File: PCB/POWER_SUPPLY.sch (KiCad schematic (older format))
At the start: 12 parts

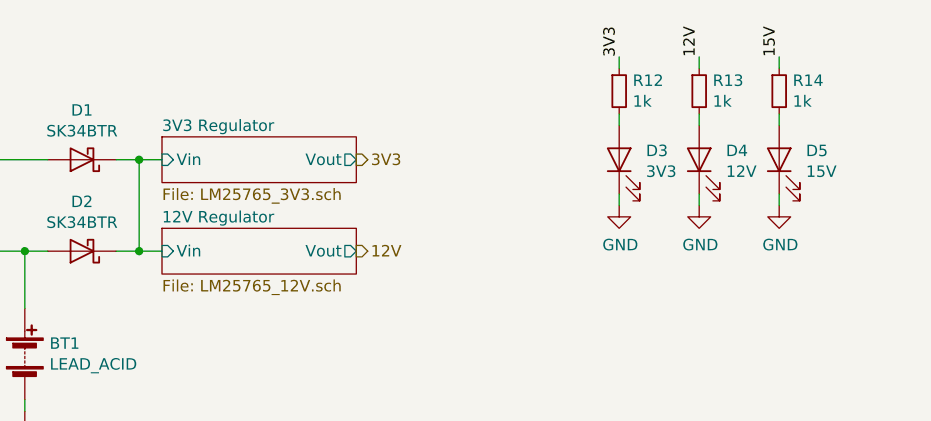
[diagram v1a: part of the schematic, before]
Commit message: Replaced 3v3 regulator with 5v
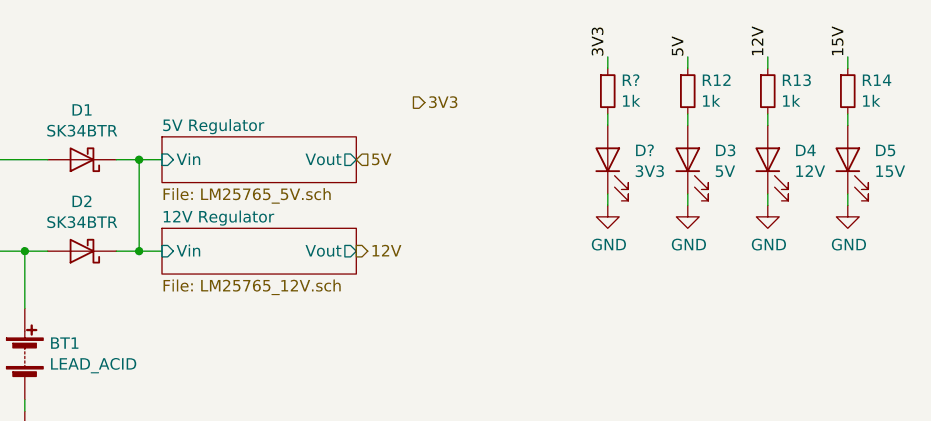
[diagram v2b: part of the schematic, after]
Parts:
- added D?: 3V3, symbol Device:LED
- added R?: 1k, symbol Device:R_Small
- D3: value 3V3 -> 5V
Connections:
- net 3V3: now also R?.1; no longer R12.1
- net GND: now also D?.1 (K)
- new net: D?.2 (A), R?.2
- new net 5V: R12.1
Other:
- moved on the sheet: D3, D4, D5, R12, R13, R14
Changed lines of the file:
@@
 $Descr A4 11693 8268
 encoding utf-8
-Sheet 9 25
+Sheet 10 25
 Title ""
 Date ""
@@
 Wire Wire Line
 	5600 3200 5700 3200
-Text HLabel 7050 2800 2    50   Output ~ 0
+Text HLabel 7300 2550 2    50   Output ~ 0
 3V3
 $Sheet
 S 6200 2700 850  200
 U 5E9C913B
-F0 "3V3 Regulator" 50
-F1 "LM25765_3V3.sch" 50
+F0 "5V Regulator" 50
+F1 "LM25765_5V.sch" 50
 F2 "Vout" O R 7050 2800 50
 F3 "Vin" I L 6200 2800 50
@@
 L Device:LED D3
 U 1 1 5E8B2580
-P 8200 2800
-F 0 "D3" V 8239 2683 50  0000 R CNN
-F 1 "3V3" V 8148 2683 50  0000 R CNN
-F 2 "" H 8200 2800 50  0001 C CNN
-F 3 "" H 8200 2800 50  0001 C CNN
-	1    8200 2800
+P 8500 2800
+F 0 "D3" V 8539 2683 50  0000 R CNN
+F 1 "5V" V 8448 2683 50  0000 R CNN
+F 2 "" H 8500 2800 50  0001 C CNN
+F 3 "" H 8500 2800 50  0001 C CNN
+	1    8500 2800
 	0    -1   -1   0
 $EndComp
@@
 L Device:R_Small R12
 U 1 1 5E8B32F4
-P 8200 2500
-F 0 "R12" H 8259 2546 50  0000 L CNN
-F 1 "1k" H 8259 2455 50  0000 L CNN
-F 2 "" H 8200 2500 50  0001 C CNN
-F 3 "" H 8200 2500 50  0001 C CNN
-	1    8200 2500
-	1    0    0    -1
-$EndComp
-Wire Wire Line
-	8200 2600 8200 2650
+P 8500 2500
+F 0 "R12" H 8559 2546 50  0000 L CNN
+F 1 "1k" H 8559 2455 50  0000 L CNN
+F 2 "" H 8500 2500 50  0001 C CNN
+F 3 "" H 8500 2500 50  0001 C CNN
+	1    8500 2500
+	1    0    0    -1
+$EndComp
+Wire Wire Line
+	8500 2600 8500 2650
 $Comp
 L power:GND #PWR067
 U 1 1 5E8B38F1
-P 8200 3000
-F 0 "#PWR067" H 8200 2750 50  0001 C CNN
-F 1 "GND" H 8205 2827 50  0000 C CNN
-F 2 "" H 8200 3000 50  0001 C CNN
-F 3 "" H 8200 3000 50  0001 C CNN
-	1    8200 3000
-	1    0    0    -1
-$EndComp
-Wire Wire Line
-	8200 2950 8200 3000
+P 8500 3000
+F 0 "#PWR067" H 8500 2750 50  0001 C CNN
+F 1 "GND" H 8505 2827 50  0000 C CNN
+F 2 "" H 8500 3000 50  0001 C CNN
+F 3 "" H 8500 3000 50  0001 C CNN
+	1    8500 3000
+	1    0    0    -1
+$EndComp
+Wire Wire Line
+	8500 2950 8500 3000
 $Comp
 L Device:LED D4
 U 1 1 5E8B5AE6
-P 8550 2800
-F 0 "D4" V 8589 2683 50  0000 R CNN
-F 1 "12V" V 8498 2683 50  0000 R CNN
-F 2 "" H 8550 2800 50  0001 C CNN
-F 3 "" H 8550 2800 50  0001 C CNN
-	1    8550 2800
+P 8850 2800
+F 0 "D4" V 8889 2683 50  0000 R CNN
+F 1 "12V" V 8798 2683 50  0000 R CNN
+F 2 "" H 8850 2800 50  0001 C CNN
+F 3 "" H 8850 2800 50  0001 C CNN
+	1    8850 2800
 	0    -1   -1   0
 $EndComp
@@
 L Device:R_Small R13
 U 1 1 5E8B5AEC
-P 8550 2500
-F 0 "R13" H 8609 2546 50  0000 L CNN
-F 1 "1k" H 8609 2455 50  0000 L CNN
-F 2 "" H 8550 2500 50  0001 C CNN
-F 3 "" H 8550 2500 50  0001 C CNN
-	1    8550 2500
-	1    0    0    -1
-$EndComp
-Wire Wire Line
-	8550 2600 8550 2650
+P 8850 2500
+F 0 "R13" H 8909 2546 50  0000 L CNN
+F 1 "1k" H 8909 2455 50  0000 L CNN
+F 2 "" H 8850 2500 50  0001 C CNN
+F 3 "" H 8850 2500 50  0001 C CNN
+	1    8850 2500
+	1    0    0    -1
+$EndComp
+Wire Wire Line
+	8850 2600 8850 2650
 $Comp
 L power:GND #PWR068
 U 1 1 5E8B5AF3
-P 8550 3000
-F 0 "#PWR068" H 8550 2750 50  0001 C CNN
-F 1 "GND" H 8555 2827 50  0000 C CNN
-F 2 "" H 8550 3000 50  0001 C CNN
-F 3 "" H 8550 3000 50  0001 C CNN
-	1    8550 3000
-	1    0    0    -1
-$EndComp
-Wire Wire Line
-	8550 2950 8550 3000
-Text Label 8200 2350 1    50   ~ 0
-3V3
-Wire Wire Line
-	8200 2350 8200 2400
-Text Label 8550 2350 1    50   ~ 0
+P 8850 3000
+F 0 "#PWR068" H 8850 2750 50  0001 C CNN
+F 1 "GND" H 8855 2827 50  0000 C CNN
+F 2 "" H 8850 3000 50  0001 C CNN
+F 3 "" H 8850 3000 50  0001 C CNN
+	1    8850 3000
+	1    0    0    -1
+$EndComp
+Wire Wire Line
+	8850 2950 8850 3000
+Text Label 8500 2350 1    50   ~ 0
+5V
+Wire Wire Line
+	8500 2350 8500 2400
+Text Label 8850 2350 1    50   ~ 0
 12V
 Wire Wire Line
-	8550 2350 8550 2400
+	8850 2350 8850 2400
 Connection ~ 6100 3200
 Wire Wire Line
@@
 L Device:LED D5
 U 1 1 5E8B6ACE
-P 8900 2800
-F 0 "D5" V 8939 2683 50  0000 R CNN
-F 1 "15V" V 8848 2683 50  0000 R CNN
-F 2 "" H 8900 2800 50  0001 C CNN
-F 3 "" H 8900 2800 50  0001 C CNN
-	1    8900 2800
+P 9200 2800
+F 0 "D5" V 9239 2683 50  0000 R CNN
+F 1 "15V" V 9148 2683 50  0000 R CNN
+F 2 "" H 9200 2800 50  0001 C CNN
+F 3 "" H 9200 2800 50  0001 C CNN
+	1    9200 2800
 	0    -1   -1   0
 $EndComp
@@
 L Device:R_Small R14
 U 1 1 5E8B6AD4
-P 8900 2500
-F 0 "R14" H 8959 2546 50  0000 L CNN
-F 1 "1k" H 8959 2455 50  0000 L CNN
-F 2 "" H 8900 2500 50  0001 C CNN
-F 3 "" H 8900 2500 50  0001 C CNN
-	1    8900 2500
-	1    0    0    -1
-$EndComp
-Wire Wire Line
-	8900 2600 8900 2650
+P 9200 2500
+F 0 "R14" H 9259 2546 50  0000 L CNN
+F 1 "1k" H 9259 2455 50  0000 L CNN
+F 2 "" H 9200 2500 50  0001 C CNN
+F 3 "" H 9200 2500 50  0001 C CNN
+	1    9200 2500
+	1    0    0    -1
+$EndComp
+Wire Wire Line
+	9200 2600 9200 2650
 $Comp
 L power:GND #PWR069
 U 1 1 5E8B6ADB
-P 8900 3000
-F 0 "#PWR069" H 8900 2750 50  0001 C CNN
-F 1 "GND" H 8905 2827 50  0000 C CNN
-F 2 "" H 8900 3000 50  0001 C CNN
-F 3 "" H 8900 3000 50  0001 C CNN
-	1    8900 3000
-	1    0    0    -1
-$EndComp
-Wire Wire Line
-	8900 2950 8900 3000
-Text Label 8900 2350 1    50   ~ 0
+P 9200 3000
+F 0 "#PWR069" H 9200 2750 50  0001 C CNN
+F 1 "GND" H 9205 2827 50  0000 C CNN
+F 2 "" H 9200 3000 50  0001 C CNN
+F 3 "" H 9200 3000 50  0001 C CNN
+	1    9200 3000
+	1    0    0    -1
+$EndComp
+Wire Wire Line
+	9200 2950 9200 3000
+Text Label 9200 2350 1    50   ~ 0
 15V
 Wire Wire Line
-	8900 2350 8900 2400
+	9200 2350 9200 2400
 Text Label 3750 2800 0    50   ~ 0
 15V
+Text HLabel 7050 2800 2    50   Input ~ 0
+5V
+$Comp
+L Device:LED D?
+U 1 1 5E8FE8F5
+P 8150 2800
+F 0 "D?" V 8189 2683 50  0000 R CNN
+F 1 "3V3" V 8098 2683 50  0000 R CNN
+F 2 "" H 8150 2800 50  0001 C CNN
+F 3 "" H 8150 2800 50  0001 C CNN
+	1    8150 2800
+	0    -1   -1   0
+$EndComp
+$Comp
+L Device:R_Small R?
+U 1 1 5E8FE8FB
+P 8150 2500
+F 0 "R?" H 8209 2546 50  0000 L CNN
+F 1 "1k" H 8209 2455 50  0000 L CNN
+F 2 "" H 8150 2500 50  0001 C CNN
+F 3 "" H 8150 2500 50  0001 C CNN
+	1    8150 2500
+	1    0    0    -1
+$EndComp
+Wire Wire Line
+	8150 2600 8150 2650
+$Comp
+L power:GND #PWR?
+U 1 1 5E8FE902
+P 8150 3000
+F 0 "#PWR?" H 8150 2750 50  0001 C CNN
+F 1 "GND" H 8155 2827 50  0000 C CNN
+F 2 "" H 8150 3000 50  0001 C CNN
+F 3 "" H 8150 3000 50  0001 C CNN
+	1    8150 3000
+	1    0    0    -1
+$EndComp
+Wire Wire Line
+	8150 2950 8150 3000
+Text Label 8150 2350 1    50   ~ 0
+3V3
+Wire Wire Line
+	8150 2350 8150 2400
 $EndSCHEMATC

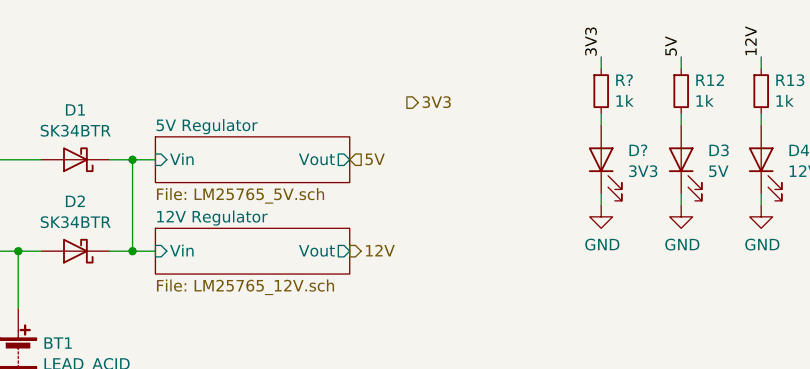
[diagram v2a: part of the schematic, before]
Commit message: Increased VCC from 3v3 to 5v
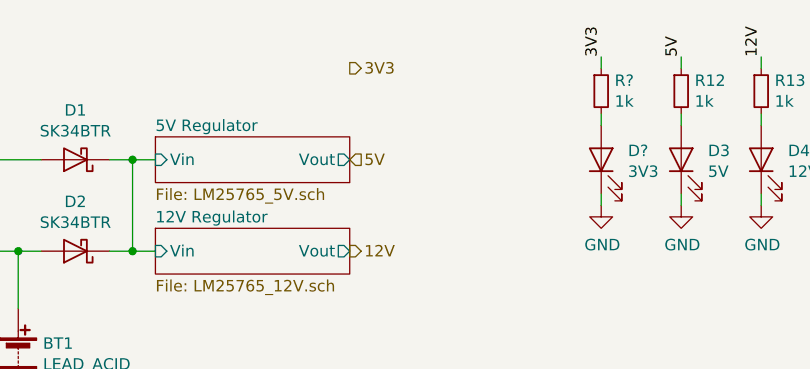
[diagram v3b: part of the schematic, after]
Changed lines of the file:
@@
 Wire Wire Line
 	5600 3200 5700 3200
-Text HLabel 7300 2550 2    50   Output ~ 0
+Text HLabel 7050 2400 2    50   Output ~ 0
 3V3
 $Sheet

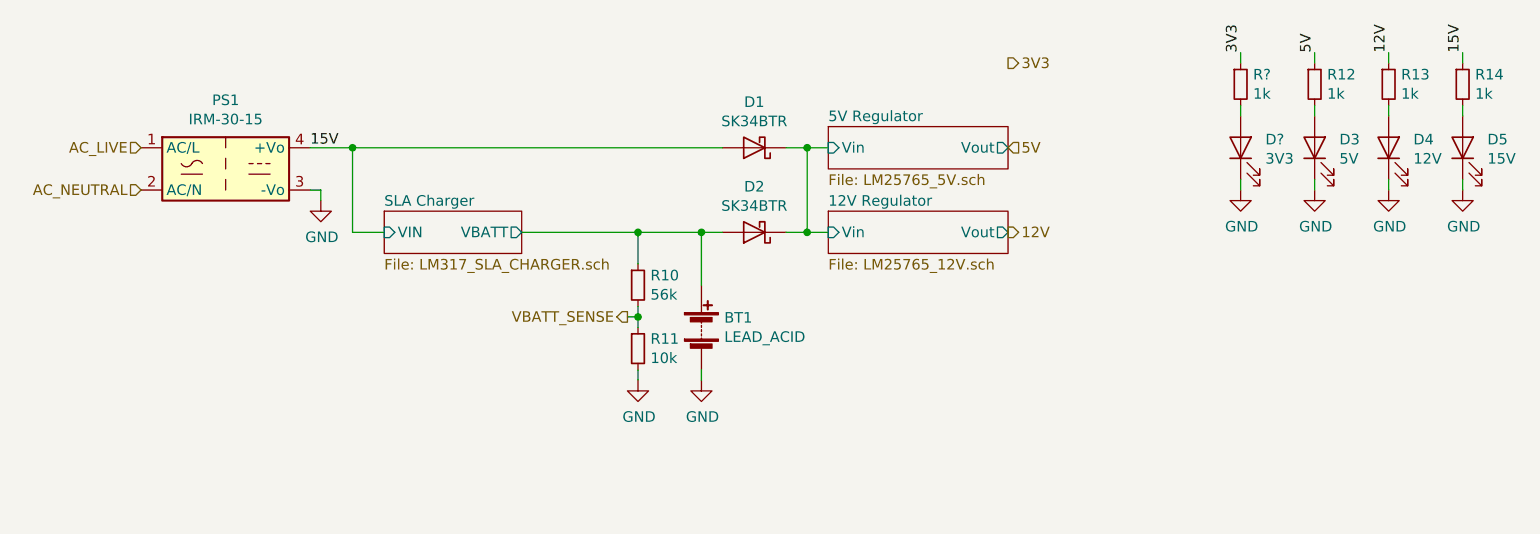
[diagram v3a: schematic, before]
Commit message: Added Humidity and temperature sensors
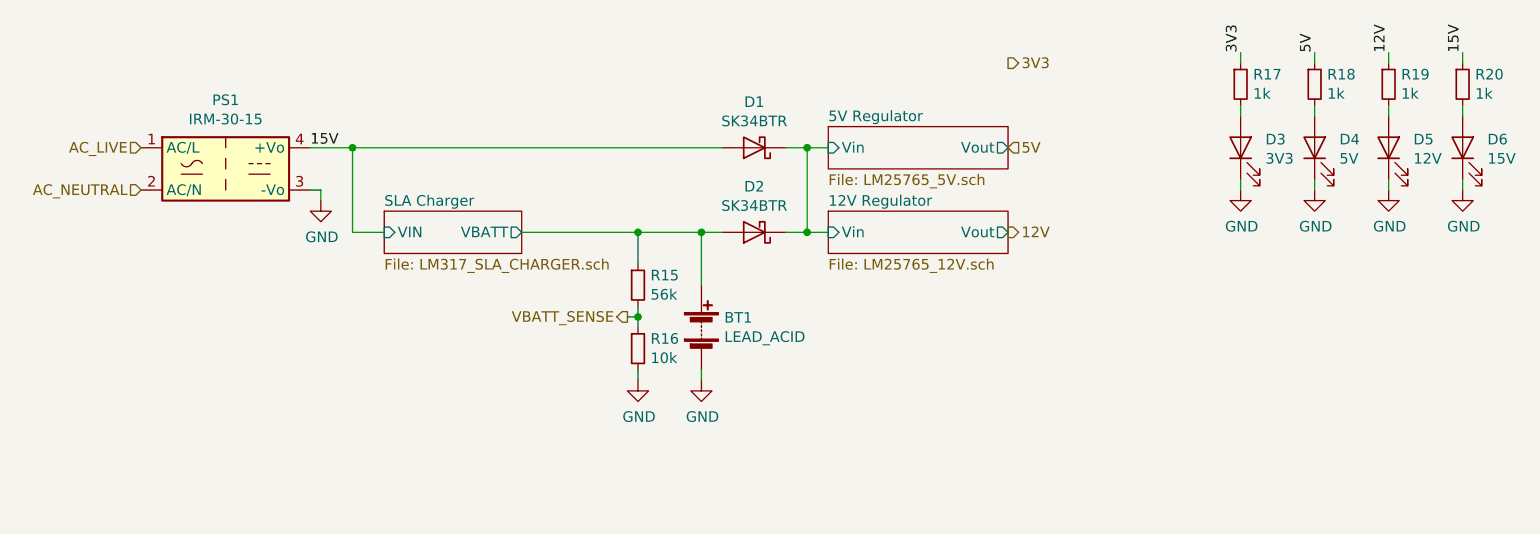
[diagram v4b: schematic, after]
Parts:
- gave numbers to parts that had none: 2
- renumbered D3 to D4, D4 to D5, D5 to D6, R10 to R15, R11 to R16, R12 to R18, R13 to R19, R14 to R20
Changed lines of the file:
@@
 	5600 3200 5600 3450
 $Comp
-L power:GND #PWR066
+L power:GND #PWR068
 U 1 1 5E929E4E
 P 5600 3900
-F 0 "#PWR066" H 5600 3650 50  0001 C CNN
+F 0 "#PWR068" H 5600 3650 50  0001 C CNN
 F 1 "GND" H 5605 3727 50  0000 C CNN
 F 2 "" H 5600 3900 50  0001 C CNN
@@
 Connection ~ 3950 2800
 $Comp
-L power:GND #PWR064
+L power:GND #PWR066
 U 1 1 5E92F162
 P 3800 3050
-F 0 "#PWR064" H 3800 2800 50  0001 C CNN
+F 0 "#PWR066" H 3800 2800 50  0001 C CNN
 F 1 "GND" H 3805 2877 50  0000 C CNN
 F 2 "" H 3800 3050 50  0001 C CNN
@@
 VBATT_SENSE
 $Comp
-L Device:R_Small R11
+L Device:R_Small R16
 U 1 1 5E987A48
 P 5300 3750
-F 0 "R11" H 5359 3796 50  0000 L CNN
+F 0 "R16" H 5359 3796 50  0000 L CNN
 F 1 "10k" H 5359 3705 50  0000 L CNN
 F 2 "" H 5300 3750 50  0001 C CNN
@@
 Connection ~ 5300 3600
 $Comp
-L power:GND #PWR065
+L power:GND #PWR067
 U 1 1 5E989430
 P 5300 3900
-F 0 "#PWR065" H 5300 3650 50  0001 C CNN
+F 0 "#PWR067" H 5300 3650 50  0001 C CNN
 F 1 "GND" H 5305 3727 50  0000 C CNN
 F 2 "" H 5300 3900 50  0001 C CNN
@@
 	5300 3850 5300 3900
 $Comp
-L Device:R_Small R10
+L Device:R_Small R15
 U 1 1 5E98794C
 P 5300 3450
-F 0 "R10" H 5359 3496 50  0000 L CNN
+F 0 "R15" H 5359 3496 50  0000 L CNN
 F 1 "56k" H 5359 3405 50  0000 L CNN
 F 2 "" H 5300 3450 50  0001 C CNN
@@
 Connection ~ 6100 2800
 $Comp
-L Device:LED D3
+L Device:LED D4
 U 1 1 5E8B2580
 P 8500 2800
-F 0 "D3" V 8539 2683 50  0000 R CNN
+F 0 "D4" V 8539 2683 50  0000 R CNN
 F 1 "5V" V 8448 2683 50  0000 R CNN
 F 2 "" H 8500 2800 50  0001 C CNN
@@
 $EndComp
 $Comp
-L Device:R_Small R12
+L Device:R_Small R18
 U 1 1 5E8B32F4
 P 8500 2500
-F 0 "R12" H 8559 2546 50  0000 L CNN
+F 0 "R18" H 8559 2546 50  0000 L CNN
 F 1 "1k" H 8559 2455 50  0000 L CNN
 F 2 "" H 8500 2500 50  0001 C CNN
@@
 	8500 2600 8500 2650
 $Comp
-L power:GND #PWR067
+L power:GND #PWR070
 U 1 1 5E8B38F1
 P 8500 3000
-F 0 "#PWR067" H 8500 2750 50  0001 C CNN
+F 0 "#PWR070" H 8500 2750 50  0001 C CNN
 F 1 "GND" H 8505 2827 50  0000 C CNN
 F 2 "" H 8500 3000 50  0001 C CNN
@@
 	8500 2950 8500 3000
 $Comp
-L Device:LED D4
+L Device:LED D5
 U 1 1 5E8B5AE6
 P 8850 2800
-F 0 "D4" V 8889 2683 50  0000 R CNN
+F 0 "D5" V 8889 2683 50  0000 R CNN
 F 1 "12V" V 8798 2683 50  0000 R CNN
 F 2 "" H 8850 2800 50  0001 C CNN
@@
 $EndComp
 $Comp
-L Device:R_Small R13
+L Device:R_Small R19
 U 1 1 5E8B5AEC
 P 8850 2500
-F 0 "R13" H 8909 2546 50  0000 L CNN
+F 0 "R19" H 8909 2546 50  0000 L CNN
 F 1 "1k" H 8909 2455 50  0000 L CNN
 F 2 "" H 8850 2500 50  0001 C CNN
@@
 	8850 2600 8850 2650
 $Comp
-L power:GND #PWR068
+L power:GND #PWR071
 U 1 1 5E8B5AF3
 P 8850 3000
-F 0 "#PWR068" H 8850 2750 50  0001 C CNN
+F 0 "#PWR071" H 8850 2750 50  0001 C CNN
 F 1 "GND" H 8855 2827 50  0000 C CNN
 F 2 "" H 8850 3000 50  0001 C CNN
@@
 	6100 3200 6200 3200
 $Comp
-L Device:LED D5
+L Device:LED D6
 U 1 1 5E8B6ACE
 P 9200 2800
-F 0 "D5" V 9239 2683 50  0000 R CNN
+F 0 "D6" V 9239 2683 50  0000 R CNN
 F 1 "15V" V 9148 2683 50  0000 R CNN
 F 2 "" H 9200 2800 50  0001 C CNN
@@
 $EndComp
 $Comp
-L Device:R_Small R14
+L Device:R_Small R20
 U 1 1 5E8B6AD4
 P 9200 2500
-F 0 "R14" H 9259 2546 50  0000 L CNN
+F 0 "R20" H 9259 2546 50  0000 L CNN
 F 1 "1k" H 9259 2455 50  0000 L CNN
 F 2 "" H 9200 2500 50  0001 C CNN
@@
 	9200 2600 9200 2650
 $Comp
-L power:GND #PWR069
+L power:GND #PWR072
 U 1 1 5E8B6ADB
 P 9200 3000
-F 0 "#PWR069" H 9200 2750 50  0001 C CNN
+F 0 "#PWR072" H 9200 2750 50  0001 C CNN
 F 1 "GND" H 9205 2827 50  0000 C CNN
 F 2 "" H 9200 3000 50  0001 C CNN
@@
 5V
 $Comp
-L Device:LED D?
+L Device:LED D3
 U 1 1 5E8FE8F5
 P 8150 2800
-F 0 "D?" V 8189 2683 50  0000 R CNN
+F 0 "D3" V 8189 2683 50  0000 R CNN
 F 1 "3V3" V 8098 2683 50  0000 R CNN
 F 2 "" H 8150 2800 50  0001 C CNN
@@
 $EndComp
 $Comp
-L Device:R_Small R?
+L Device:R_Small R17
 U 1 1 5E8FE8FB
 P 8150 2500
-F 0 "R?" H 8209 2546 50  0000 L CNN
+F 0 "R17" H 8209 2546 50  0000 L CNN
 F 1 "1k" H 8209 2455 50  0000 L CNN
 F 2 "" H 8150 2500 50  0001 C CNN
@@
 	8150 2600 8150 2650
 $Comp
-L power:GND #PWR?
+L power:GND #PWR069
 U 1 1 5E8FE902
 P 8150 3000
-F 0 "#PWR?" H 8150 2750 50  0001 C CNN
+F 0 "#PWR069" H 8150 2750 50  0001 C CNN
 F 1 "GND" H 8155 2827 50  0000 C CNN
 F 2 "" H 8150 3000 50  0001 C CNN

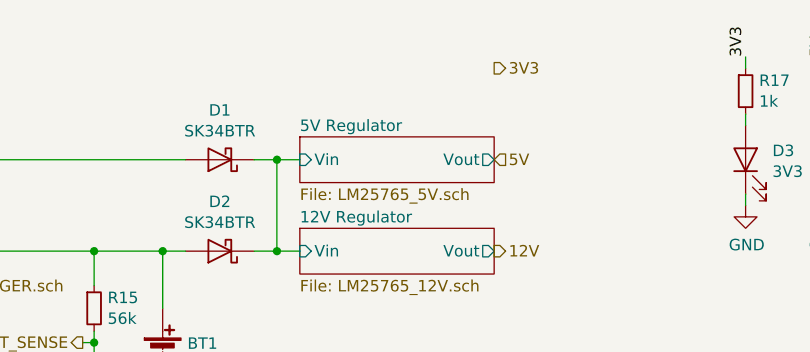
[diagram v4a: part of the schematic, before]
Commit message: Added 3V3 regulator
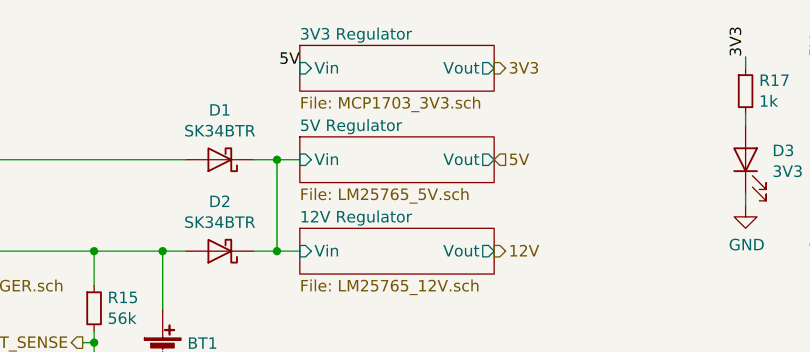
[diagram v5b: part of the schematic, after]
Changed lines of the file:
@@
 $Descr A4 11693 8268
 encoding utf-8
-Sheet 10 25
+Sheet 10 26
 Title ""
 Date ""
@@
 Wire Wire Line
 	8850 2950 8850 3000
-Text Label 8500 2350 1    50   ~ 0
-5V
 Wire Wire Line
 	8500 2350 8500 2400
@@
 Wire Wire Line
 	8150 2350 8150 2400
+$Sheet
+S 6200 2300 850  200
+U 5E940C9C
+F0 "3V3 Regulator" 50
+F1 "MCP1703_3V3.sch" 50
+F2 "Vin" I L 6200 2400 50
+F3 "Vout" O R 7050 2400 50
+$EndSheet
+Text Label 8500 2350 1    50   ~ 0
+5V
+Text Label 6200 2400 2    50   ~ 0
+5V
 $EndSCHEMATC
